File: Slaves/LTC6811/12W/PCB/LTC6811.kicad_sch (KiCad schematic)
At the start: 56 parts, among them J1 Cells, J2 PB MB, J3 PA MA, J4 Temp, Q1 NSV1C201MZ4, U1 LTC6811-1

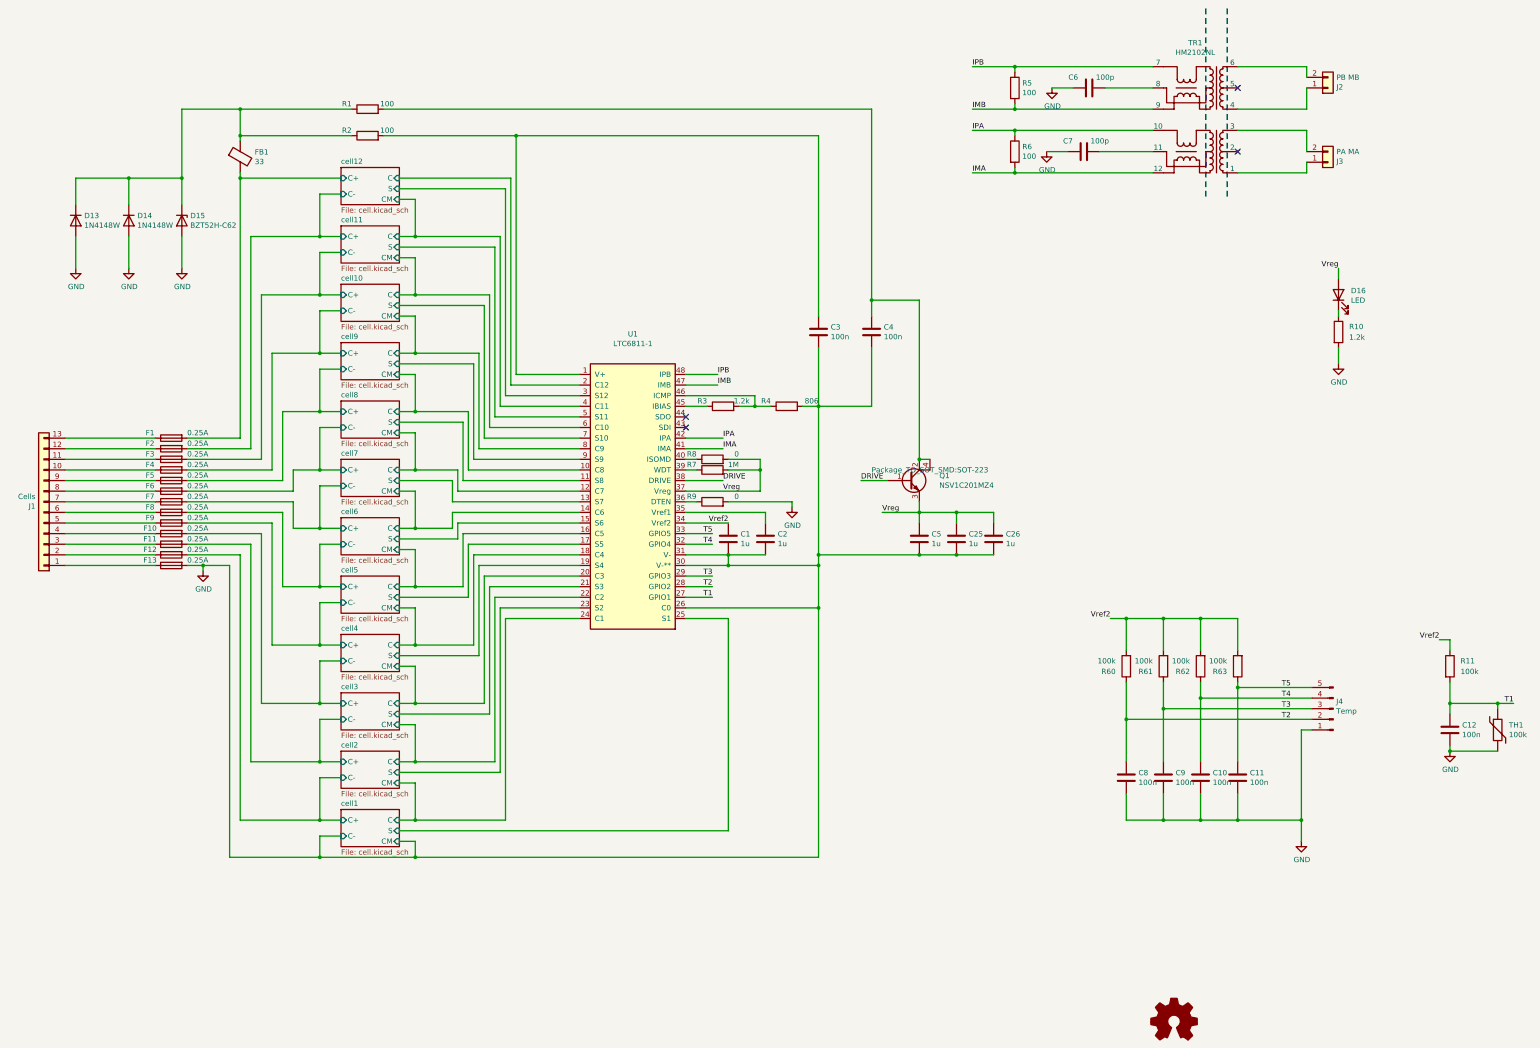
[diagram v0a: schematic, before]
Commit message: Finish most routing
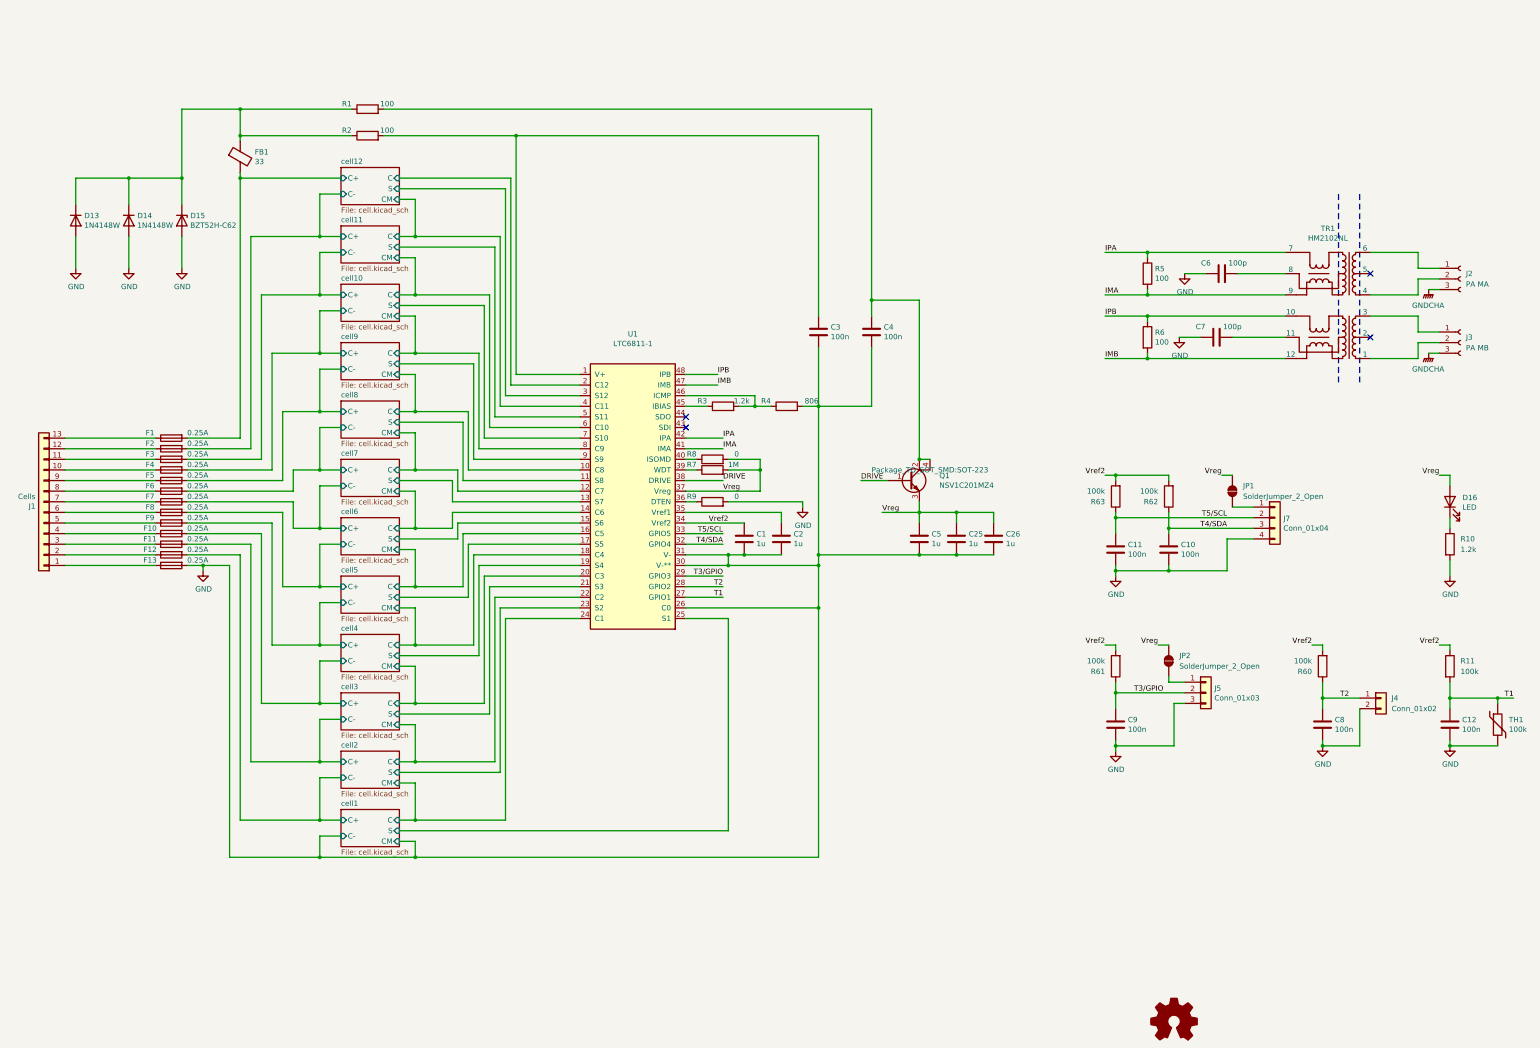
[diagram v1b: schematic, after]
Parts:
- removed J2: PB MB, ENNOID:Pin_1x02-XL, symbol Connector_Generic:Conn_01x02
- removed J3: PA MA, ENNOID:Pin_1x02-XL, symbol Connector_Generic:Conn_01x02
- removed J4: Temp, Connector_PinHeader_2.54mm:PinHeader_1x05_P2.54mm_Horizontal, symbol LTC6811-rescue:Conn_01x05_Male-Connector
- added J2: PA MA, symbol Connector:Conn_01x03_Socket
- added J3: PA MB, Connector_PinSocket_1.27mm:PinSocket_1x03_P1.27mm_Vertical, symbol Connector:Conn_01x03_Socket
- added J4: Conn_01x02, Connector_PinHeader_1.27mm:PinHeader_1x02_P1.27mm_Horizontal, symbol Connector_Generic:Conn_01x02
- added J5: Conn_01x03, Connector_PinHeader_1.27mm:PinHeader_1x03_P1.27mm_Horizontal, symbol Connector_Generic:Conn_01x03
- added J7: Conn_01x04, Connector_PinHeader_1.27mm:PinHeader_1x04_P1.27mm_Horizontal, symbol Connector_Generic:Conn_01x04
- added JP1, JP2: SolderJumper_2_Open, Jumper:SolderJumper-2_P1.3mm_Open_Pad1.0x1.5mm, symbol Jumper:SolderJumper_2_Open
- C1, C2: footprint Capacitor_SMD:C_0805_2012Metric -> Capacitor_SMD:C_0603_1608Metric
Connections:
- net T5 is gone; now on net T5/SCL: C11.1, R63.1, U1.33 (NC)
- net GND: now also J4.2 (Pin_2), J5.3 (Pin_3), J7.4 (Pin_4)
- net IMA: now also R5.2, TR1.9; no longer R6.2, TR1.12
- net IMB: now also R6.2, TR1.12; no longer R5.2, TR1.9
- net IPA: now also R5.1, TR1.7; no longer R6.1, TR1.10
- net IPB: now also R6.1, TR1.10; no longer R5.1, TR1.7
- net T2: now also J4.1 (Pin_1)
- net Vreg: now also JP1.2 (B), JP2.2 (B)
- net at TR1.1: now also J3.2 (Pin_2)
- net at TR1.3: now also J3.1 (Pin_1)
- net at TR1.4: now also J2.2 (Pin_2)
- net at TR1.6: now also J2.1 (Pin_1)
- net T5/SCL: now reaches U1.33 (NC)
- net T5/SCL: now also J7.2 (Pin_2)
- net T3 renamed T3/GPIO
- net T3/GPIO: now also J5.2 (Pin_2)
- net T4 renamed T4/SDA
- net T4/SDA: now also J7.3 (Pin_3)
- new net: J5.1 (Pin_1), JP2.1 (A)
- new net: J7.1 (Pin_1), JP1.1 (A)
- new net GNDCHA: J2.3 (Pin_3), J3.3 (Pin_3)
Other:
- moved on the sheet: C1, C12, C2, C6, C7, C8, D16, R10, R5, R6, R60, TH1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

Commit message: Finish Rev1
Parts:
- J3: footprint Connector_PinSocket_1.27mm:PinSocket_1x03_P1.27mm_Vertical -> Connector_PinSocket_2.54mm:PinSocket_1x03_P2.54mm_Horizontal
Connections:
- net at TR1.1: now also J3.1 (Pin_1); no longer J3.2 (Pin_2)
- net at TR1.3: now also J3.2 (Pin_2); no longer J3.1 (Pin_1)
- net at TR1.4: now also J2.1 (Pin_1); no longer J2.2 (Pin_2)
- net at TR1.6: now also J2.2 (Pin_2); no longer J2.1 (Pin_1)
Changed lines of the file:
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@@
 	(wire
 		(pts
-			(xy 358.14 101.6) (xy 369.57 101.6)
+			(xy 358.14 101.6) (xy 367.03 101.6)
 		)
 		(stroke
@@
 	(wire
 		(pts
-			(xy 369.57 101.6) (xy 369.57 97.79)
+			(xy 367.03 95.25) (xy 367.03 101.6)
 		)
 		(stroke
@@
 	(wire
 		(pts
-			(xy 142.24 114.3) (xy 129.54 114.3)
+			(xy 369.57 91.44) (xy 369.57 97.79)
 		)
 		(stroke
@@
 	(wire
 		(pts
-			(xy 129.54 212.09) (xy 151.13 212.09)
+			(xy 142.24 114.3) (xy 129.54 114.3)
 		)
 		(stroke
@@
 	(wire
 		(pts
-			(xy 106.68 104.14) (xy 106.68 114.3)
+			(xy 129.54 212.09) (xy 151.13 212.09)
 		)
 		(stroke
@@
 	(wire
 		(pts
-			(xy 129.54 142.24) (xy 125.73 142.24)
+			(xy 106.68 104.14) (xy 106.68 114.3)
 		)
 		(stroke
@@
 	(wire
 		(pts
-			(xy 369.57 80.01) (xy 374.65 80.01)
+			(xy 129.54 142.24) (xy 125.73 142.24)
 		)
 		(stroke
@@
 	(wire
 		(pts
-			(xy 369.57 97.79) (xy 374.65 97.79)
-		)
-		(stroke
-			(width 0)
-			(type default)
-		)
-	)
-	(wire
-		(pts
 			(xy 106.68 104.14) (xy 111.76 104.14)
 		)
@@
 	(wire
 		(pts
-			(xy 369.57 95.25) (xy 374.65 95.25)
-		)
-		(stroke
-			(width 0)
-			(type default)
-		)
-	)
-	(wire
-		(pts
-			(xy 369.57 76.2) (xy 369.57 80.01)
+			(xy 369.57 76.2) (xy 369.57 82.55)
 		)
 		(stroke
@@
 	(wire
 		(pts
+			(xy 367.03 95.25) (xy 374.65 95.25)
+		)
+		(stroke
+			(width 0)
+			(type default)
+		)
+	)
+	(wire
+		(pts
 			(xy 144.78 172.72) (xy 144.78 151.13)
 		)
@@
 	(wire
 		(pts
+			(xy 374.65 80.01) (xy 367.03 80.01)
+		)
+		(stroke
+			(width 0)
+			(type default)
+		)
+	)
+	(wire
+		(pts
 			(xy 313.69 81.28) (xy 318.77 81.28)
 		)
@@
 	(wire
 		(pts
-			(xy 369.57 91.44) (xy 369.57 95.25)
-		)
-		(stroke
-			(width 0)
-			(type default)
-		)
-	)
-	(wire
-		(pts
 			(xy 346.71 182.88) (xy 346.71 179.07)
 		)
@@
 	(wire
 		(pts
+			(xy 369.57 82.55) (xy 374.65 82.55)
+		)
+		(stroke
+			(width 0)
+			(type default)
+		)
+	)
+	(wire
+		(pts
 			(xy 377.19 182.88) (xy 377.19 185.42)
 		)
@@
 	(wire
 		(pts
-			(xy 358.14 86.36) (xy 369.57 86.36)
+			(xy 358.14 86.36) (xy 367.03 86.36)
 		)
 		(stroke
@@
 	(wire
 		(pts
+			(xy 369.57 97.79) (xy 374.65 97.79)
+		)
+		(stroke
+			(width 0)
+			(type default)
+		)
+	)
+	(wire
+		(pts
 			(xy 168.91 123.19) (xy 144.78 123.19)
 		)
@@
 	(wire
 		(pts
-			(xy 369.57 82.55) (xy 369.57 86.36)
+			(xy 367.03 80.01) (xy 367.03 86.36)
 		)
 		(stroke
@@
 	(wire
 		(pts
-			(xy 369.57 82.55) (xy 374.65 82.55)
-		)
-		(stroke
-			(width 0)
-			(type default)
-		)
-	)
-	(wire
-		(pts
 			(xy 121.92 41.91) (xy 238.76 41.91)
 		)
@@
 			)
 		)
-		(property "Footprint" "Connector_PinSocket_1.27mm:PinSocket_1x03_P1.27mm_Vertical"
+		(property "Footprint" "Connector_PinSocket_2.54mm:PinSocket_1x03_P2.54mm_Horizontal"
 			(at 379.73 97.79 0)
 			(effects

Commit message: more updates
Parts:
- removed C10, C11, C9: 100n, Capacitor_SMD:C_0603_1608Metric, symbol Device:C
- removed J2: PA MA, symbol Connector:Conn_01x03_Socket
- removed J3: PA MB, Connector_PinSocket_2.54mm:PinSocket_1x03_P2.54mm_Horizontal, symbol Connector:Conn_01x03_Socket
- removed J5: Conn_01x03, Connector_PinHeader_1.27mm:PinHeader_1x03_P1.27mm_Horizontal, symbol Connector_Generic:Conn_01x03
- removed J7: Conn_01x04, Connector_PinHeader_1.27mm:PinHeader_1x04_P1.27mm_Horizontal, symbol Connector_Generic:Conn_01x04
- removed JP1, JP2: SolderJumper_2_Open, Jumper:SolderJumper-2_P1.3mm_Open_Pad1.0x1.5mm, symbol Jumper:SolderJumper_2_Open
- removed R61, R62, R63: 100k, Resistor_SMD:R_0603_1608Metric, symbol Device:R
- added J2: Conn_01x06, Connector_PinHeader_2.00mm:PinHeader_1x06_P2.00mm_Vertical, symbol Connector_Generic:Conn_01x06
- added J4, J5: Conn_01x02, Connector_JST:JST_XA_S02B-XASK-1_1x02_P2.50mm_Horizontal, symbol Connector_Generic:Conn_01x02
- added R8: 0, Resistor_SMD:R_1206_3216Metric, symbol Device:R
- C1, C2: MPN CL21B105KBFNNNE -> GMK107AB7105KAHT
- C5: footprint Capacitor_SMD:C_0805_2012Metric -> Capacitor_SMD:C_0603_1608Metric; MPN CL21B105KBFNNNE -> GMK107AB7105KAHT
- C6: renamed from C25; footprint Capacitor_SMD:C_0805_2012Metric -> Capacitor_SMD:C_0603_1608Metric; MPN CL21B105KBFNNNE -> GMK107AB7105KAHT
- C7: renamed from C26; footprint Capacitor_SMD:C_0805_2012Metric -> Capacitor_SMD:C_0603_1608Metric; MPN CL21B105KBFNNNE -> GMK107AB7105KAHT
- F1, F10, F11, F12, F13, F2, F3, F4, F5, F6, F7, F8, F9: MPN N/A -> 0438.250WRA
- J1, LOGO1: MPN N/A -> (none); now left out of the parts list
- J3: renamed from J4; footprint Connector_PinHeader_1.27mm:PinHeader_1x02_P1.27mm_Horizontal -> Connector_JST:JST_XA_S02B-XASK-1_1x02_P2.50mm_Horizontal; MPN (none) -> B02B-XASK-1
- TH1: footprint Resistor_SMD:R_0805_2012Metric -> Resistor_SMD:R_0603_1608Metric; MPN SDNT2012X104F4250FTF -> NCU18WF104F6SRB
- renumbered C8 to C10, C12 to C11, C7 to C8, C6 to C9, D13 to D1, D14 to D2, D15 to D3, D16 to D4, R6 to R10, R5 to R11, R60 to R12, R11 to R13, R8 to R3, R7 to R4, R9 to R5, R3 to R6, R4 to R7, R10 to R9
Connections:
- net GND: now also J2.6 (Pin_6)
- net IMA: now also R10.1, TR1.7; no longer R11.2, TR1.9
- net IMB: now also R11.1, TR1.10; no longer R10.2, TR1.12
- net IPA: now also R10.2, TR1.9; no longer R11.1, TR1.7
- net IPB: now also R11.2, TR1.12; no longer R10.1, TR1.10
- net T3/GPIO: now also J2.5 (Pin_5)
- net T4/SDA: now also J2.4 (Pin_4)
- net T5/SCL: now also J2.3 (Pin_3)
- net Vref2: now also J2.2 (Pin_2)
- net Vreg: now also J2.1 (Pin_1), R8.2; no longer C6.1, C7.1, D4.2 (A), Q1.3 (E)
- net at TR1.1: now also J5.1 (Pin_1)
- net at TR1.3: now also J5.2 (Pin_2)
- net at TR1.4: now also J4.1 (Pin_1)
- net at TR1.6: now also J4.2 (Pin_2)
- new net: C6.1, C7.1, D4.2 (A), Q1.3 (E), R8.1
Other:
- moved on the sheet: C5, C6, C7, D4, R10, R11, R9
